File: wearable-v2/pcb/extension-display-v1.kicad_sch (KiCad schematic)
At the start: 2 parts, among them J5 EXT_4_SOCKET, U10 ATmega328PB-M

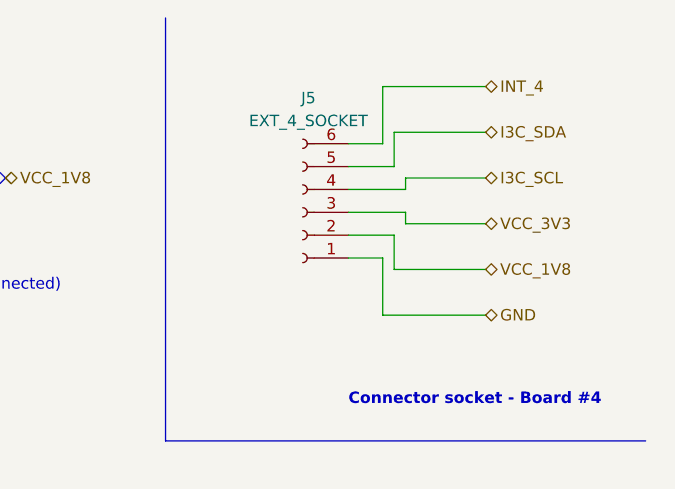
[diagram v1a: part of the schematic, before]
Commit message: Added front connectors on main board
Signed-off-by: Adam Fowler <adam@adamfowler.org>
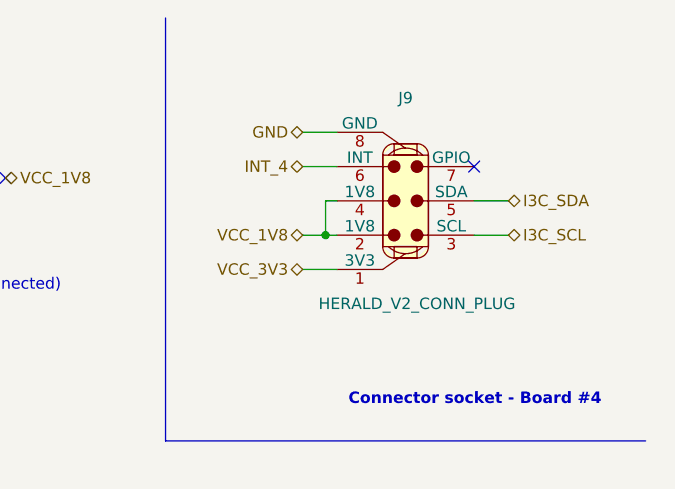
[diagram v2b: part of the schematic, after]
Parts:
- removed J5: EXT_4_SOCKET, symbol Connector:Conn_01x06_Socket
- added J9: HERALD_V2_CONN_PLUG, symbol Herald_Extras:HERALD_V2_CONN_PLUG
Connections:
- net GND: now also J9.8 (GND)
- net I3C_SCL: now also J9.3 (SCL)
- net I3C_SDA: now also J9.5 (SDA)
- net INT_4: now also J9.6 (INT)
- net VCC_1V8: now also J9.2 (1V8), J9.4 (1V8)
- net VCC_3V3: now also J9.1 (3V3)
- no-connect marks 7 -> 8
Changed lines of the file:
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@@
   (junction (at 153.67 96.52) (diameter 0) (color 0 0 0 0)
   )
+  (junction (at 247.65 38.1) (diameter 0) (color 0 0 0 0)
+  )
   (junction (at 69.85 22.86) (diameter 0) (color 0 0 0 0)
   )
   (no_connect (at 175.26 66.04))
+  (no_connect (at 264.16 30.48))
   (no_connect (at 175.26 62.23))
   (no_connect (at 175.26 58.42))
@@
     (stroke (width 0) (type default))
   )
-  (wire (pts (xy 250.19 27.94) (xy 254 27.94))
-    (stroke (width 0) (type default))
-  )
   (wire (pts (xy 167.64 111.76) (xy 175.26 111.76))
     (stroke (width 0) (type default))
@@
     (stroke (width 0) (type default))
   )
-  (wire (pts (xy 265.43 46.99) (xy 254 46.99))
-    (stroke (width 0) (type default))
-  )
   (wire (pts (xy 167.64 107.95) (xy 175.26 107.95))
     (stroke (width 0) (type default))
@@
     (stroke (width 0) (type default))
   )
-  (wire (pts (xy 255.27 38.1) (xy 250.19 38.1))
-    (stroke (width 0) (type default))
-  )
   (wire (pts (xy 82.55 46.99) (xy 90.17 46.99))
     (stroke (width 0) (type default))
@@
     (stroke (width 0) (type default))
   )
-  (wire (pts (xy 265.43 21.59) (xy 254 21.59))
-    (stroke (width 0) (type default))
-  )
-  (wire (pts (xy 265.43 26.67) (xy 255.27 26.67))
-    (stroke (width 0) (type default))
-  )
   (wire (pts (xy 165.1 81.28) (xy 175.26 81.28))
     (stroke (width 0) (type default))
   )
+  (wire (pts (xy 245.11 41.91) (xy 248.92 41.91))
+    (stroke (width 0) (type default))
+  )
   (wire (pts (xy 167.64 34.29) (xy 175.26 34.29))
     (stroke (width 0) (type default))
@@
     (stroke (width 0) (type default))
   )
-  (wire (pts (xy 254 21.59) (xy 254 27.94))
-    (stroke (width 0) (type default))
-  )
   (wire (pts (xy 82.55 59.69) (xy 90.17 59.69))
     (stroke (width 0) (type default))
@@
     (stroke (width 0) (type default))
   )
-  (wire (pts (xy 265.43 31.75) (xy 256.54 31.75))
+  (wire (pts (xy 264.16 34.29) (xy 267.97 34.29))
     (stroke (width 0) (type default))
   )
@@
     (stroke (width 0) (type default))
   )
-  (wire (pts (xy 256.54 31.75) (xy 256.54 33.02))
-    (stroke (width 0) (type default))
-  )
-  (wire (pts (xy 250.19 30.48) (xy 255.27 30.48))
+  (wire (pts (xy 248.92 34.29) (xy 247.65 34.29))
     (stroke (width 0) (type default))
   )
@@
     (stroke (width 0) (type default))
   )
-  (wire (pts (xy 256.54 35.56) (xy 256.54 36.83))
-    (stroke (width 0) (type default))
-  )
-  (wire (pts (xy 254 46.99) (xy 254 40.64))
-    (stroke (width 0) (type default))
-  )
-  (wire (pts (xy 255.27 41.91) (xy 255.27 38.1))
+  (wire (pts (xy 247.65 34.29) (xy 247.65 38.1))
+    (stroke (width 0) (type default))
+  )
+  (wire (pts (xy 245.11 38.1) (xy 247.65 38.1))
     (stroke (width 0) (type default))
   )
@@
     (stroke (width 0) (type default))
   )
-  (wire (pts (xy 265.43 41.91) (xy 255.27 41.91))
-    (stroke (width 0) (type default))
-  )
   (wire (pts (xy 67.31 26.67) (xy 67.31 22.86))
     (stroke (width 0) (type default))
@@
     (stroke (width 0) (type default))
   )
+  (wire (pts (xy 245.11 30.48) (xy 248.92 30.48))
+    (stroke (width 0) (type default))
+  )
   (wire (pts (xy 167.64 22.86) (xy 175.26 22.86))
     (stroke (width 0) (type default))
@@
     (stroke (width 0) (type default))
   )
-  (wire (pts (xy 256.54 36.83) (xy 265.43 36.83))
+  (wire (pts (xy 245.11 26.67) (xy 248.92 26.67))
     (stroke (width 0) (type default))
   )
@@
     (stroke (width 0) (type default))
   )
-  (wire (pts (xy 250.19 33.02) (xy 256.54 33.02))
-    (stroke (width 0) (type default))
-  )
   (wire (pts (xy 82.55 67.31) (xy 90.17 67.31))
     (stroke (width 0) (type default))
@@
     (stroke (width 0) (type default))
   )
-  (wire (pts (xy 255.27 26.67) (xy 255.27 30.48))
-    (stroke (width 0) (type default))
-  )
   (wire (pts (xy 82.55 82.55) (xy 90.17 82.55))
     (stroke (width 0) (type default))
   )
-  (wire (pts (xy 254 40.64) (xy 250.19 40.64))
+  (wire (pts (xy 247.65 38.1) (xy 248.92 38.1))
     (stroke (width 0) (type default))
   )
@@
     (stroke (width 0) (type default))
   )
-  (wire (pts (xy 250.19 35.56) (xy 256.54 35.56))
-    (stroke (width 0) (type default))
-  )
   (polyline (pts (xy 13.97 111.76) (xy 114.3 111.76))
     (stroke (width 0) (type default))
   )
   (wire (pts (xy 67.31 22.86) (xy 69.85 22.86))
+    (stroke (width 0) (type default))
+  )
+  (wire (pts (xy 264.16 38.1) (xy 267.97 38.1))
     (stroke (width 0) (type default))
   )
@@
     (effects (font (size 1.27 1.27)) (justify left))
   )
-  (hierarchical_label "INT_4" (shape bidirectional) (at 265.43 21.59 0) (fields_autoplaced)
-    (effects (font (size 1.27 1.27)) (justify left))
+  (hierarchical_label "INT_4" (shape bidirectional) (at 245.11 30.48 180) (fields_autoplaced)
+    (effects (font (size 1.27 1.27)) (justify right))
   )
   (hierarchical_label "GND" (shape bidirectional) (at 45.72 187.96 0) (fields_autoplaced)
@@
     (effects (font (size 1.27 1.27)) (justify right))
   )
-  (hierarchical_label "I3C_SCL" (shape bidirectional) (at 265.43 31.75 0) (fields_autoplaced)
+  (hierarchical_label "I3C_SCL" (shape bidirectional) (at 267.97 38.1 0) (fields_autoplaced)
     (effects (font (size 1.27 1.27)) (justify left))
   )
@@
     (effects (font (size 1.27 1.27)) (justify right))
   )
-  (hierarchical_label "VCC_3V3" (shape bidirectional) (at 265.43 36.83 0) (fields_autoplaced)
-    (effects (font (size 1.27 1.27)) (justify left))
-  )
-  (hierarchical_label "GND" (shape bidirectional) (at 265.43 46.99 0) (fields_autoplaced)
-    (effects (font (size 1.27 1.27)) (justify left))
+  (hierarchical_label "VCC_3V3" (shape bidirectional) (at 245.11 41.91 180) (fields_autoplaced)
+    (effects (font (size 1.27 1.27)) (justify right))
+  )
+  (hierarchical_label "GND" (shape bidirectional) (at 245.11 26.67 180) (fields_autoplaced)
+    (effects (font (size 1.27 1.27)) (justify right))
   )
   (hierarchical_label "VCC_3V3" (shape bidirectional) (at 167.64 30.48 180) (fields_autoplaced)
@@
     (effects (font (size 1.27 1.27)) (justify right))
   )
-  (hierarchical_label "VCC_1V8" (shape bidirectional) (at 265.43 41.91 0) (fields_autoplaced)
-    (effects (font (size 1.27 1.27)) (justify left))
-  )
-  (hierarchical_label "I3C_SDA" (shape bidirectional) (at 265.43 26.67 0) (fields_autoplaced)
+  (hierarchical_label "VCC_1V8" (shape bidirectional) (at 245.11 38.1 180) (fields_autoplaced)
+    (effects (font (size 1.27 1.27)) (justify right))
+  )
+  (hierarchical_label "I3C_SDA" (shape bidirectional) (at 267.97 34.29 0) (fields_autoplaced)
     (effects (font (size 1.27 1.27)) (justify left))
   )
@@
     (effects (font (size 1.27 1.27)) (justify left))
   )
-  (symbol (lib_id "Connector:Conn_01x06_Socket") (at 245.11 35.56 180) (unit 1)
-    (in_bom yes) (on_board yes) (dnp no) (fields_autoplaced)
-    (property "Reference" "J5" (at 245.745 22.86 0)
+  (symbol (lib_id "Herald_Extras:HERALD_V2_CONN_PLUG") (at 256.54 34.29 0) (unit 1)
+    (in_bom yes) (on_board yes) (dnp no)
+    (property "Reference" "J9" (at 256.54 22.86 0)
       (effects (font (size 1.27 1.27)))
     )
-    (property "Value" "EXT_4_SOCKET" (at 245.745 25.4 0)
+    (property "Value" "HERALD_V2_CONN_PLUG" (at 257.81 45.72 0)
       (effects (font (size 1.27 1.27)))
     )
-    (property "Footprint" "" (at 245.11 35.56 0)
+    (property "Footprint" "" (at 256.54 30.48 0)
       (effects (font (size 1.27 1.27)) hide)
     )
-    (property "Datasheet" "~" (at 245.11 35.56 0)
+    (property "Datasheet" "https://ele.kyocera.com/assets/products/connector/specification/201035861003.pdf" (at 257.81 49.53 0)
       (effects (font (size 1.27 1.27)) hide)
     )
@@
     (pin "5")
     (pin "6")
+    (pin "7")
+    (pin "8")
     (instances
       (project "wearable-v2"
-        (path "/1eb7e8c9-86dc-4f6b-85aa-748b782af952/88c842d7-ac9a-4ec4-bd18-165411775e80"
-          (reference "J5") (unit 1)
-        )
-        (path "/1eb7e8c9-86dc-4f6b-85aa-748b782af952/23d45666-f217-4505-adda-dcfbc4ac09cf"
-          (reference "J6") (unit 1)
-        )
         (path "/1eb7e8c9-86dc-4f6b-85aa-748b782af952/b2450f58-45d3-4267-a96b-cde30ab720a0"
           (reference "J9") (unit 1)

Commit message: First look feedback board
Signed-off-by: Adam Fowler <adam@adamfowler.org>
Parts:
- added C12: 100nF, Capacitor_SMD:C_0402_1005Metric, symbol Device:C
- added C22: 1mF 0402, symbol Device:C
- added C23, C7: 10mF 0402, symbol Device:C
- added C32: 50nF 0402, symbol Device:C
- added C33: 250mF 0402, symbol Device:C
- added C34: C, symbol Device:C
- added C35, C36: 22pF 0402, symbol Device:C
- added R10: 10k, Resistor_SMD:R_0402_1005Metric, symbol Device:R_US
- added R5: 10 0402, Resistor_SMD:R_0402_1005Metric, symbol Device:R_US
- added R5: 1k 0402, Resistor_SMD:R_0402_1005Metric, symbol Device:R_US
- added U13: LM386, symbol Amplifier_Audio:LM386
- added U16: DRV2605LDGS, Package_SO:VSSOP-10_3x3mm_P0.5mm, symbol Driver_Haptic:DRV2605LDGS
- added U17: ~, Package_DFN_QFN:DFN-8-1EP_2x2mm_P0.5mm_EP1.05x1.75mm, symbol Herald_Extras:MAX5394
- added U7: MX25R8035FZxxx0, Herald:USON-8-1EP_2x3mm_P0.5mm_EP0.25x1.65mm, symbol Herald_Extras:MX25R8035FZxxx0
- added Y2: 16Mhz, symbol Device:Crystal
- U10: User Info (none) -> https://i.redd.it/bggdd9srui351.png
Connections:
- net AVR_RESET: now also R5.1
- net CSX: now also U10.11 (PD7); no longer U10.14 (PB2)
- net DCX: now also U17.5 (SCLK)
- net GND: now also C12.1, C22.1, C34.2, C35.1, C36.1, R5.2, U13.2 (-), U13.4 (GND), U16.8 (GND), U17.2 (GND), U17.8 (H), U17.9 (EP), U7.4 (GND), U7.EP (GND)
- net I3C_SCL: no longer U10.6 (PE1)
- net I3C_SDA: no longer U10.3 (PE0)
- net MISO1: now also U7.2 (SO/SIO1)
- net MOSI0: now also U17.4 (DIN)
- net MOSI1: now also U7.5 (SI/SIO0)
- net SCK1: now also U7.6 (SCLK)
- net SOUND_PWM: now also U10.9 (PD5), C7.1; no longer U10.30 (PD0)
- net VIBRATE_PWM: now also U16.4 (IN/TRIG)
- net FB_AUDIO_SEL: now reaches U10.12 (PB0)
- net FB_AUDIO_SEL: now also U17.3 (CS)
- net FB_FLASH_SEL: now reaches U10.13 (PB1)
- net FB_FLASH_SEL: now also U7.1 (~{CS})
- net DISPLAY_EN: now reaches U10.2 (PD4)
- net VIBRATE_EN: now reaches U10.26 (PC3)
- net VIBRATE_EN: now also U16.5 (EN)
- net FB_FTDI_RX: now reaches U10.31 (PD1)
- net at U10.7 (XTAL1/PB6): now also C35.2, Y2.2
- net at U10.8 (XTAL2/PB7): now also C36.2, Y2.1
- net VCC_3V3 renamed VDD
- net VDD: now also C12.2, C34.1, R10.1, R5.2, U13.6 (V+), U16.10 (VDD), U16.6 (VDD/NC), U17.6 (VDD), U7.8 (VCC)
- new net: C7.2, U17.1 (L)
- new net: C32.2, R5.1
- new net: C22.2, U16.1 (REG)
- new net: C23.1, U13.1 (GAIN)
- new net: C23.2, U13.8 (GAIN)
- new net: C32.1, C33.2, U13.5
- new net: U13.3 (+), U17.7 (W)
- new net FB_FLASH_RST: R10.2, U7.7 (~{RESET}/SIO3)
- new net FB_FLASH_WP: U10.14 (PB2), U7.3 (~{WP}/SIO2)
- new net FB_FTDI_TX: U10.30 (PD0)
- new net FB_SCL: U10.6 (PE1), U16.2 (SCL)
- new net FB_SDA: U10.3 (PE0), U16.3 (SDA)
- new net LRA+: U16.7 (OUT+)
- new net LRA-: U16.9 (OUT-)
- new net SPEAKER_OUT: C33.1
- no-connect marks 8 -> 11
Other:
- note added: "1V7-3V6, <10mA"
- note added: "Audio feedback"
- note added: "Display feedback"
- note added: "FTDI SERIAL DEBUG CONNECTOR"
- note added: "Feedback controller"
- note added: "Flash Memory"
- note added: "Haptic feedback"
- note added: "SPI FW DEBUG CONNECTOR"
- note added: "WARNING: GAIN OF 200!!!"
- note added: "WARNING: MIN 4V INPUT - SO NEED AN ALTERNATIVE!"
- note added: "optional"
- note removed: "DEBUG CONNECTOR"
